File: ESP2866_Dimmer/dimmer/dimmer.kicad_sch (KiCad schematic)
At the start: 56 parts, among them J1 Screw_Terminal_01x04, J10 Conn_01x16_Male, J2 Screw_Terminal_01x02, J3 Screw_Terminal_01x04, J4 Conn_01x08, J6 Conn_01x03_Male, J7 Screw_Terminal_01x02, J8 Conn_01x06, J9 Conn_01x16_Female, Q1 2N3904, Q2 DMG1012T, Q3 DMG1012T, Q4 FDD4141, SW1 Reset, SW2 Menu1, SW3 Menu2, SW4 Menu3, SW5 Menu4, SW6 Flash, U1 AP1117-33, U2 ESP-12E, U3 AP1117-50, U4 24LC01, U5 PCF8574, U6 PCF8574, U7 LCD-20X4

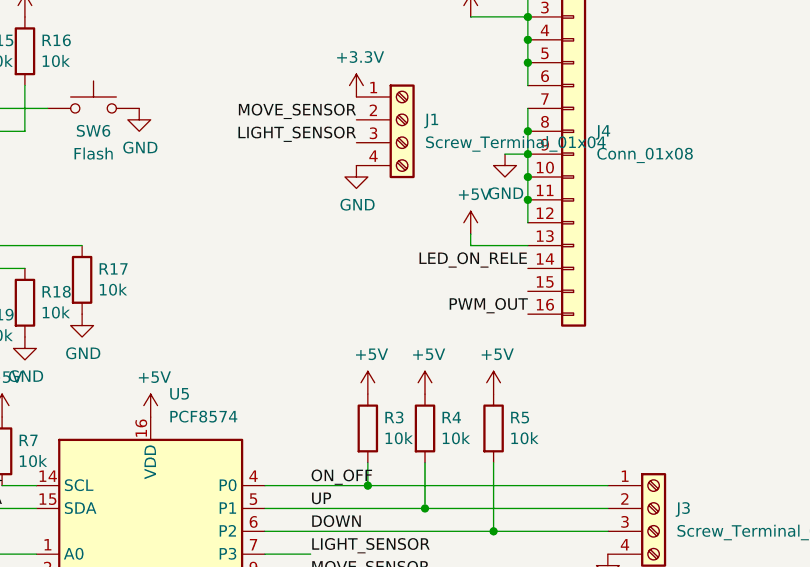
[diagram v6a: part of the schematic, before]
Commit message: Fix error in external net
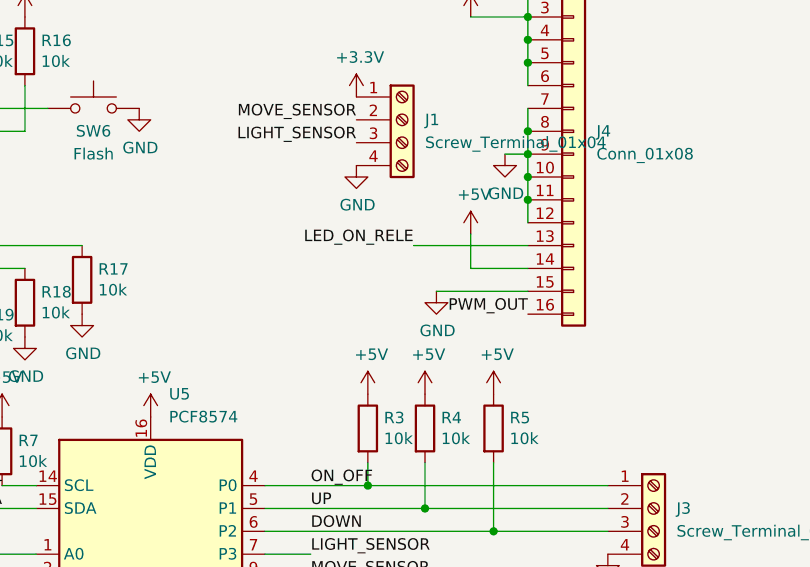
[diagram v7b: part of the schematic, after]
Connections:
- net +5V: now also J4.14 (Pin_14); no longer J4.13 (Pin_13)
- net GND: now also J4.15 (Pin_15)
- net LED_ON_RELE: now also J4.13 (Pin_13); no longer J4.14 (Pin_14)
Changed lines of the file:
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@@
+    (stroke (width 0) (type default) (color 0 0 0 0))
+  )
+  (wire (pts (xy 215.9 52.07) (xy 226.06 52.07))
     (stroke (width 0) (type default) (color 0 0 0 0))
   )
@@
     (stroke (width 0) (type default) (color 0 0 0 0))
   )
-  (wire (pts (xy 219.71 46.99) (xy 219.71 45.72))
+  (wire (pts (xy 219.71 45.72) (xy 219.71 49.53))
     (stroke (width 0) (type default) (color 0 0 0 0))
   )
@@
     (stroke (width 0) (type default) (color 0 0 0 0))
   )
-  (wire (pts (xy 226.06 46.99) (xy 219.71 46.99))
-    (stroke (width 0) (type default) (color 0 0 0 0))
-  )
   (wire (pts (xy 279.4 17.78) (xy 279.4 20.32))
     (stroke (width 0) (type default) (color 0 0 0 0))
@@
     (stroke (width 0) (type default) (color 0 0 0 0))
   )
+  (wire (pts (xy 213.36 46.99) (xy 226.06 46.99))
+    (stroke (width 0) (type default) (color 0 0 0 0))
+  )
   (wire (pts (xy 90.17 95.25) (xy 78.74 95.25))
     (stroke (width 0) (type default) (color 0 0 0 0))
@@
     (stroke (width 0) (type default) (color 0 0 0 0))
   )
+  (wire (pts (xy 219.71 49.53) (xy 226.06 49.53))
+    (stroke (width 0) (type default) (color 0 0 0 0))
+  )
   (wire (pts (xy 226.06 31.75) (xy 226.06 34.29))
     (stroke (width 0) (type default) (color 0 0 0 0))
@@
     (effects (font (size 1.27 1.27)) (justify right bottom))
   )
-  (label "LED_ON_RELE" (at 226.06 49.53 180)
+  (label "LED_ON_RELE" (at 213.36 46.99 180)
     (effects (font (size 1.27 1.27)) (justify right bottom))
   )
@@
     (pin "2")
   )
+  (symbol (lib_id "power:GND") (at 215.9 52.07 0) (unit 1)
+    (in_bom yes) (on_board yes)
+    (property "Reference" "#PWR?" (id 0) (at 215.9 58.42 0)
+      (effects (font (size 1.27 1.27)) hide)
+    )
+    (property "Value" "GND" (id 1) (at 216.027 56.4642 0))
+    (property "Footprint" "" (id 2) (at 215.9 52.07 0)
+      (effects (font (size 1.27 1.27)) hide)
+    )
+    (property "Datasheet" "" (id 3) (at 215.9 52.07 0)
+      (effects (font (size 1.27 1.27)) hide)
+    )
+    (pin "1")
+  )
   (symbol (lib_id "Device:R") (at 170.18 25.4 0) (unit 1)
     (in_bom yes) (on_board yes)
@@
       (reference "#PWR0125") (unit 1) (value "+5V") (footprint "")
     )
+    (path "/b74efaa0-4a8b-4d92-bc50-3696e94e47ee"
+      (reference "#PWR?") (unit 1) (value "GND") (footprint "")
+    )
     (path "/d313eb8e-cf40-4ef1-b0c2-bdf1a530763f"
